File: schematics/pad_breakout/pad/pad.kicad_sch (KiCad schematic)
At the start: 9 parts, among them J1 Conn_01x04_Pin, J2 Conn_01x04_Pin, J3 Conn_01x04_Pin, J4 Conn_01x04_Pin

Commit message: Works with the extender but blinks for whatever reason
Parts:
- B1:  XXX-00000 -> (none); - (none) -> XXX-00000
- GND_J1, GND_J2, GND_J3, GND_J4, J1, J2, J3, J4: footprint (none) -> -
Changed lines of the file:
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@@
       (effects (font (size 1.27 1.27)) (justify left) hide)
     )
-    (property "Footprint" "" (at 224.79 52.07 0)
+    (property "Footprint" "-" (at 224.79 52.07 0)
       (effects (font (size 1.27 1.27)) hide)
     )
@@
       (effects (font (size 1.27 1.27)) hide)
     )
-    (property "Footprint" "" (at 165.1 105.41 0)
+    (property "Footprint" "-" (at 165.1 105.41 0)
       (effects (font (size 1.27 1.27)) hide)
     )
@@
       (effects (font (size 1.27 1.27)) hide)
     )
-    (property "Footprint" "" (at 165.1 88.9 0)
+    (property "Footprint" "-" (at 165.1 88.9 0)
       (effects (font (size 1.27 1.27)) hide)
     )
@@
       (effects (font (size 1.27 1.27)) hide)
     )
-    (property "Footprint" "" (at 165.1 72.39 0)
+    (property "Footprint" "-" (at 165.1 72.39 0)
       (effects (font (size 1.27 1.27)) hide)
     )
@@
       (effects (font (size 1.27 1.27)) (justify left) hide)
     )
-    (property "Footprint" "" (at 208.28 52.07 0)
+    (property "Footprint" "-" (at 208.28 52.07 0)
       (effects (font (size 1.27 1.27)) hide)
     )
@@
       (effects (font (size 1.27 1.27)) (justify left) hide)
     )
-    (property "Footprint" "" (at 241.3 52.07 0)
+    (property "Footprint" "-" (at 241.3 52.07 0)
       (effects (font (size 1.27 1.27)) hide)
     )
@@
       (effects (font (size 1.27 1.27)) hide)
     )
-    (property "Footprint" "" (at 165.1 120.65 0)
+    (property "Footprint" "-" (at 165.1 120.65 0)
       (effects (font (size 1.27 1.27)) hide)
     )
@@
       (effects (font (size 1.27 1.27)) (justify left) hide)
     )
-    (property "Footprint" "" (at 256.54 52.07 0)
+    (property "Footprint" "-" (at 256.54 52.07 0)
       (effects (font (size 1.27 1.27)) hide)
     )
@@
       (effects (font (size 0.508 0.508)) hide)
     )
-    (property "Datasheet" "" (at 95.25 97.79 0)
-      (effects (font (size 1.27 1.27)) hide)
-    )
-    (property "" "XXX-00000" (at 95.25 153.67 0)
+    (property "Datasheet" "-" (at 95.25 97.79 0)
+      (effects (font (size 1.27 1.27)) hide)
+    )
+    (property "-" "XXX-00000" (at 95.25 153.67 0)
       (effects (font (size 1.524 1.524)))
     )

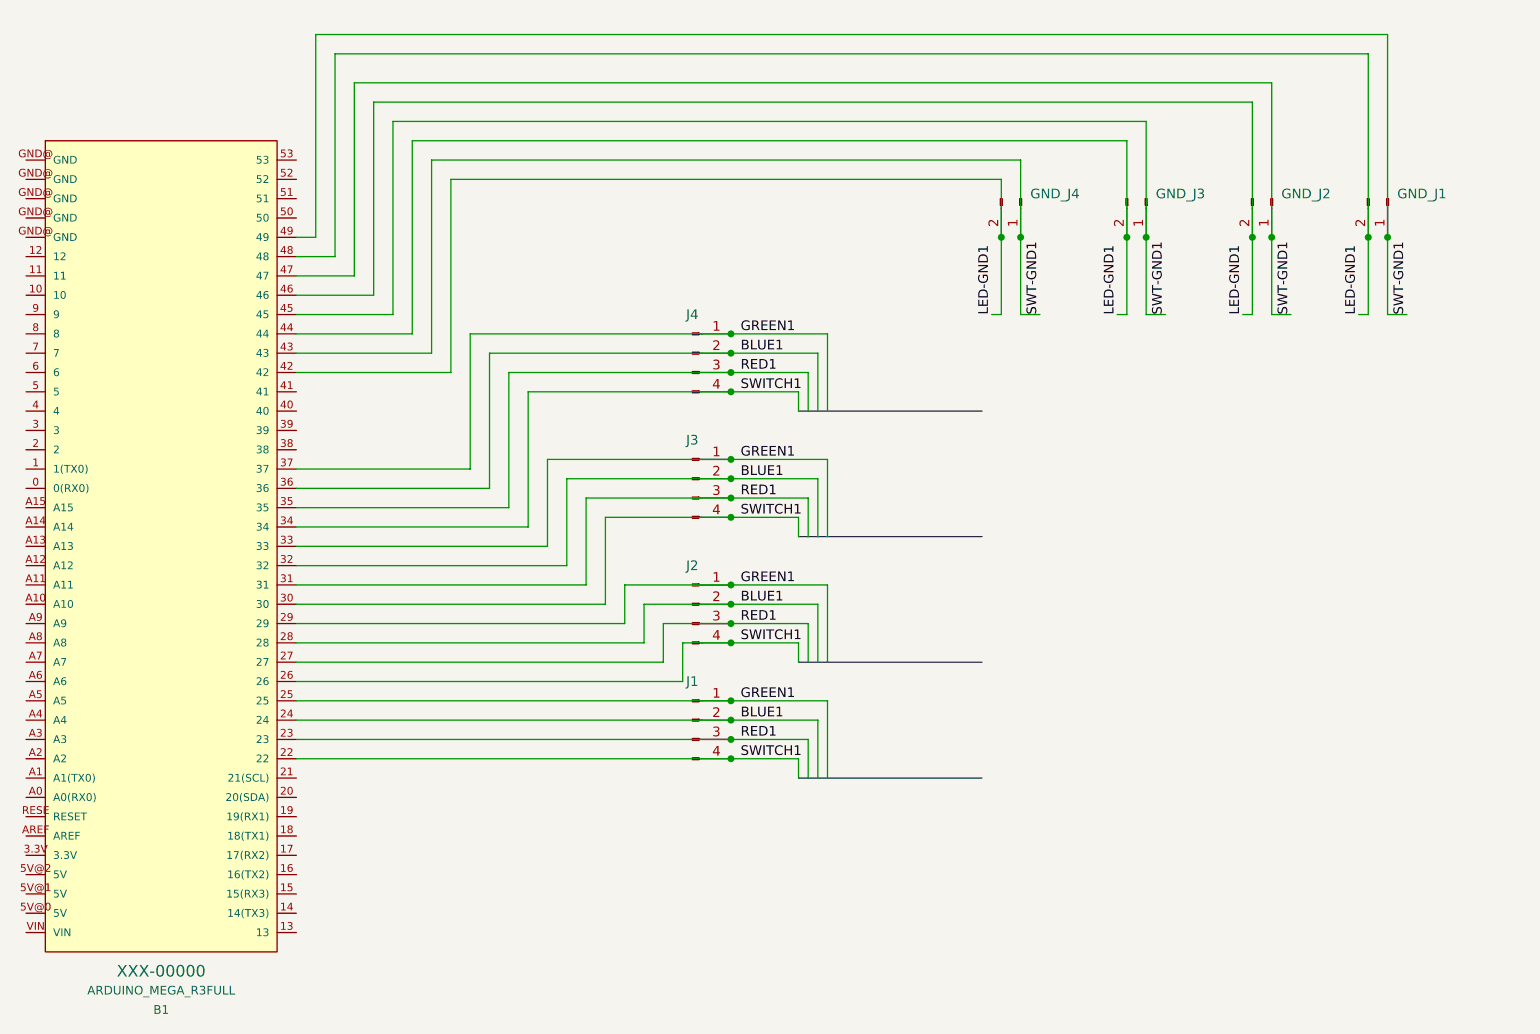
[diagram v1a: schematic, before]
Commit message: Works with the extender but blinks for whatever reason
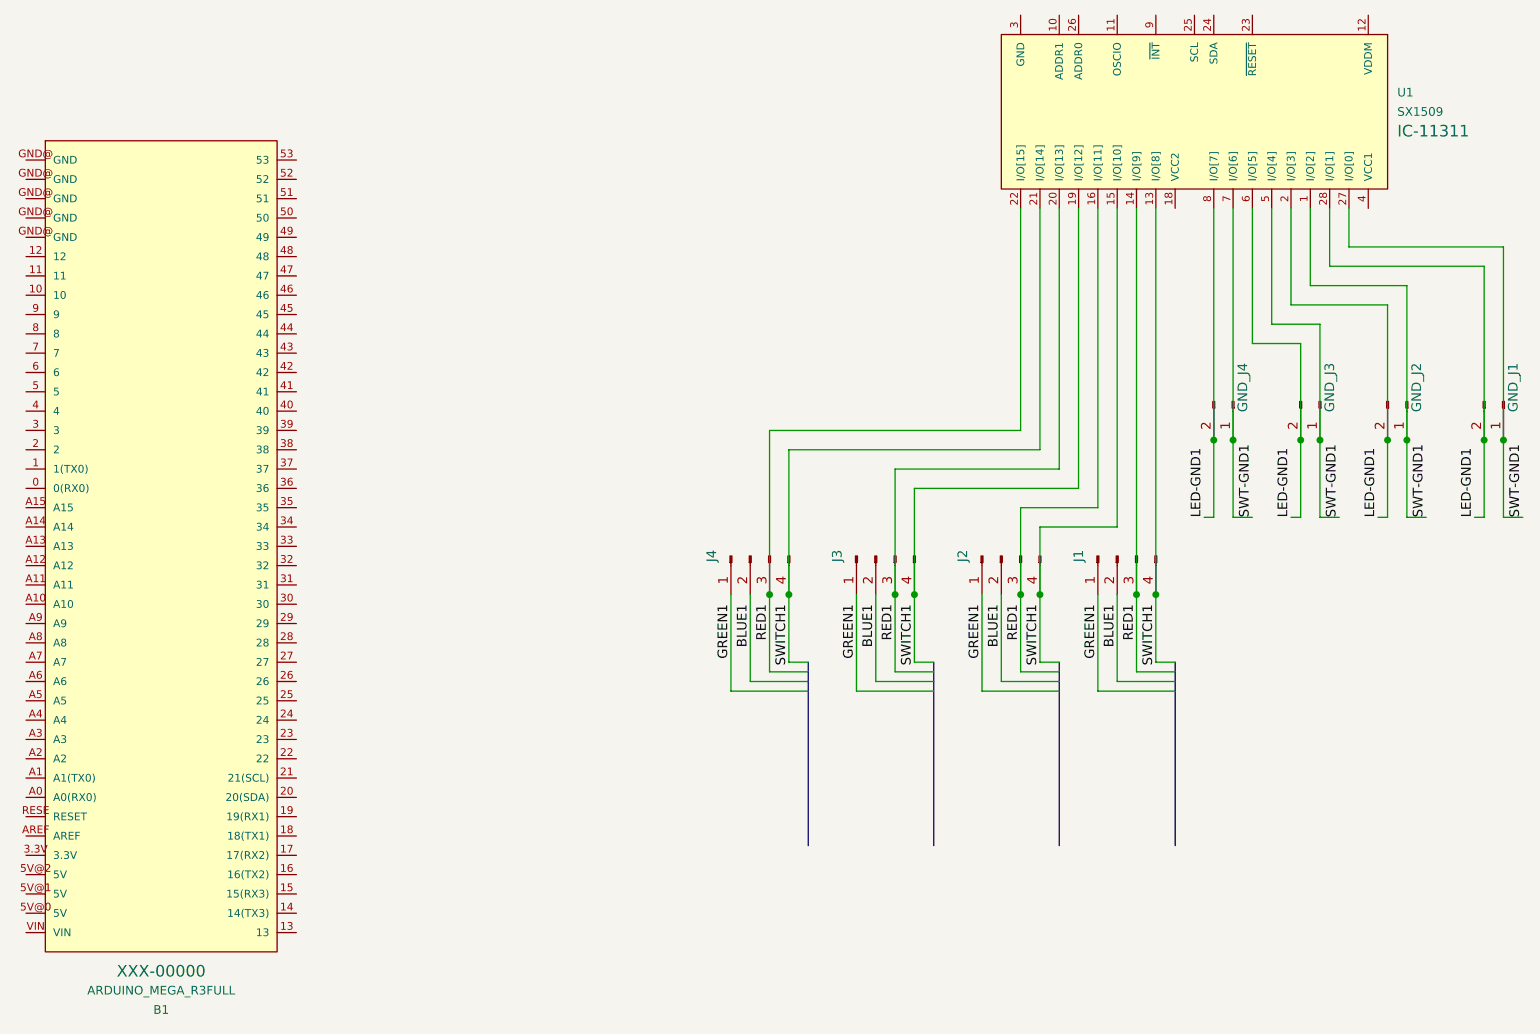
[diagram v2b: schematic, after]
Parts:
- added U1: SX1509, QFN-28, symbol SparkFun-IC-Special-Function:SX1509
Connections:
- net BLUE1: no longer B1.24, B1.28, B1.32, B1.36
- net GREEN1: no longer B1.25, B1.29, B1.33, B1.37
- net LED-GND1: now also U1.2 (I/O[3]), U1.28 (I/O[1]), U1.6 (I/O[5]), U1.8 (I/O[7]); no longer B1.42, B1.44, B1.46, B1.48
- net RED1: now also U1.14 (I/O[9]), U1.16 (I/O[11]), U1.20 (I/O[13]), U1.22 (I/O[15]); no longer B1.23, B1.27, B1.31, B1.35
- net SWITCH1: now also U1.13 (I/O[8]), U1.15 (I/O[10]), U1.19 (I/O[12]), U1.21 (I/O[14]); no longer B1.22, B1.26, B1.30, B1.34
- net SWT-GND1: now also U1.1 (I/O[2]), U1.27 (I/O[0]), U1.5 (I/O[4]), U1.7 (I/O[6]); no longer B1.43, B1.45, B1.47, B1.49
- new net: U1.17 (GND), U1.29 (GND), U1.3 (GND)
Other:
- moved on the sheet: GND_J1, GND_J2, GND_J3, GND_J4, J1, J2, J3, J4
